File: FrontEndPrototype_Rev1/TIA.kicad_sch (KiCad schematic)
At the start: 10 parts, among them U23 LTC6252, U6 ADA4807-1

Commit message: Checking if Branch Updates Work
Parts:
- gave numbers to parts that had none: 8
- renumbered U23 to U10, U6 to U11

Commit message: Small Updates
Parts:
- Rf11: renamed from Rf6; value 50k -> 39k
- renumbered Cb15 to Cb19, Cb16 to Cb20, Cf3 to Cf7, Cf4 to Cf8, R11 to R13, Rf5 to Rf10, Riso1 to Rf12, U10 to U14, U11 to U15
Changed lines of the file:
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@@
 		(on_board yes)
 		(dnp no)
-		(property "Reference" "#PWR050"
+		(property "Reference" "#PWR060"
 			(at 116.84 41.91 0)
 			(effects
@@
 		(on_board yes)
 		(dnp no)
-		(property "Reference" "Cb16"
+		(property "Reference" "Cb20"
 			(at 120.65 60.2234 90)
 			(effects
@@
 		(on_board yes)
 		(dnp no)
-		(property "Reference" "#PWR049"
+		(property "Reference" "#PWR059"
 			(at 76.2 64.77 0)
 			(effects
@@
 		(on_board yes)
 		(dnp no)
-		(property "Reference" "#PWR048"
+		(property "Reference" "#PWR058"
 			(at 62.23 39.37 0)
 			(effects
@@
 		(on_board yes)
 		(dnp no)
-		(property "Reference" "Riso1"
+		(property "Reference" "Rf12"
 			(at 135.89 51.943 90)
 			(effects
@@
 		(on_board yes)
 		(dnp no)
-		(property "Reference" "R11"
+		(property "Reference" "R13"
 			(at 102.87 49.403 90)
 			(effects
@@
 		(on_board yes)
 		(dnp no)
-		(property "Reference" "#PWR051"
+		(property "Reference" "#PWR061"
 			(at 130.81 66.04 0)
 			(effects
@@
 		(on_board yes)
 		(dnp no)
-		(property "Reference" "Cf3"
+		(property "Reference" "Cf7"
 			(at 64.77 25.9334 90)
 			(effects
@@
 		(on_board yes)
 		(dnp no)
-		(property "Reference" "U10"
+		(property "Reference" "U14"
 			(at 73.5076 53.4416 0)
 			(effects
@@
 		(on_board yes)
 		(dnp no)
-		(property "Reference" "Cf4"
+		(property "Reference" "Cf8"
 			(at 119.38 28.4734 90)
 			(effects
@@
 		(on_board yes)
 		(dnp no)
-		(property "Reference" "Cb15"
+		(property "Reference" "Cb19"
 			(at 66.04 58.9534 90)
 			(effects
@@
 		(on_board yes)
 		(dnp no)
-		(property "Reference" "#PWR047"
+		(property "Reference" "#PWR057"
 			(at 34.29 17.78 0)
 			(effects
@@
 		(on_board yes)
 		(dnp no)
-		(property "Reference" "U11"
+		(property "Reference" "U15"
 			(at 124.46 54.61 0)
 			(effects
@@
 		(on_board yes)
 		(dnp no)
-		(property "Reference" "Rf6"
+		(property "Reference" "Rf11"
 			(at 119.38 37.973 90)
 			(effects
@@
 			)
 		)
-		(property "Value" "50k"
+		(property "Value" "39k"
 			(at 119.38 40.2844 90)
 			(effects
@@
 		(on_board yes)
 		(dnp no)
-		(property "Reference" "Rf5"
+		(property "Reference" "Rf10"
 			(at 64.77 35.433 90)
 			(effects

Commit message: First Pass Schematic Fixes for Power Management Board
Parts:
- Rf?: renamed from Rf11; value 39k -> 50k
- renumbered Cb20 to Cb?, Cb19 to Cb?, Cf7 to Cf?, Cf8 to Cf?, R13 to R?, Rf12 to Rf?, Rf10 to Rf?, U14 to U23, U15 to U6

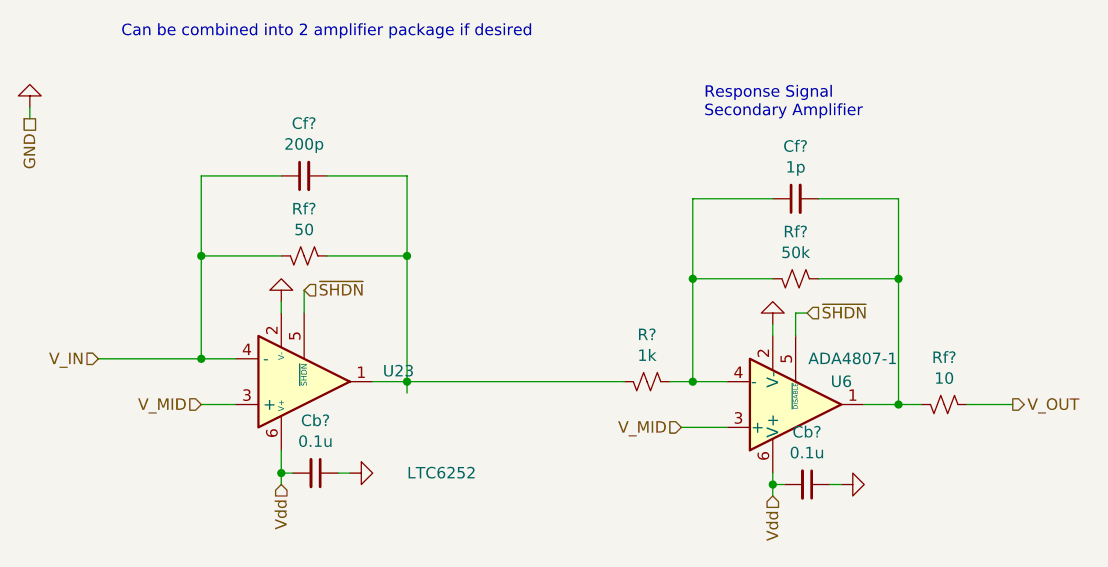
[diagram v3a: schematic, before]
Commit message: Updated Measurement Board with new 3V Reference
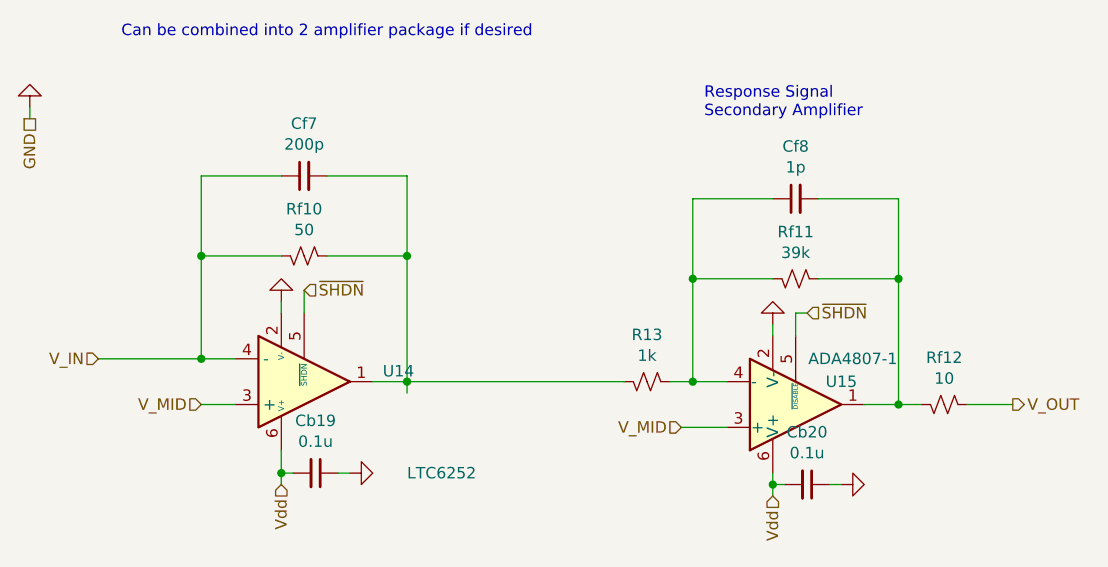
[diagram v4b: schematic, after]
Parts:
- Rf11: renamed from Rf?; value 50k -> 39k
- gave numbers to parts that had none: 7
- renumbered U23 to U14, U6 to U15
